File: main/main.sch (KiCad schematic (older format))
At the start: 0 parts

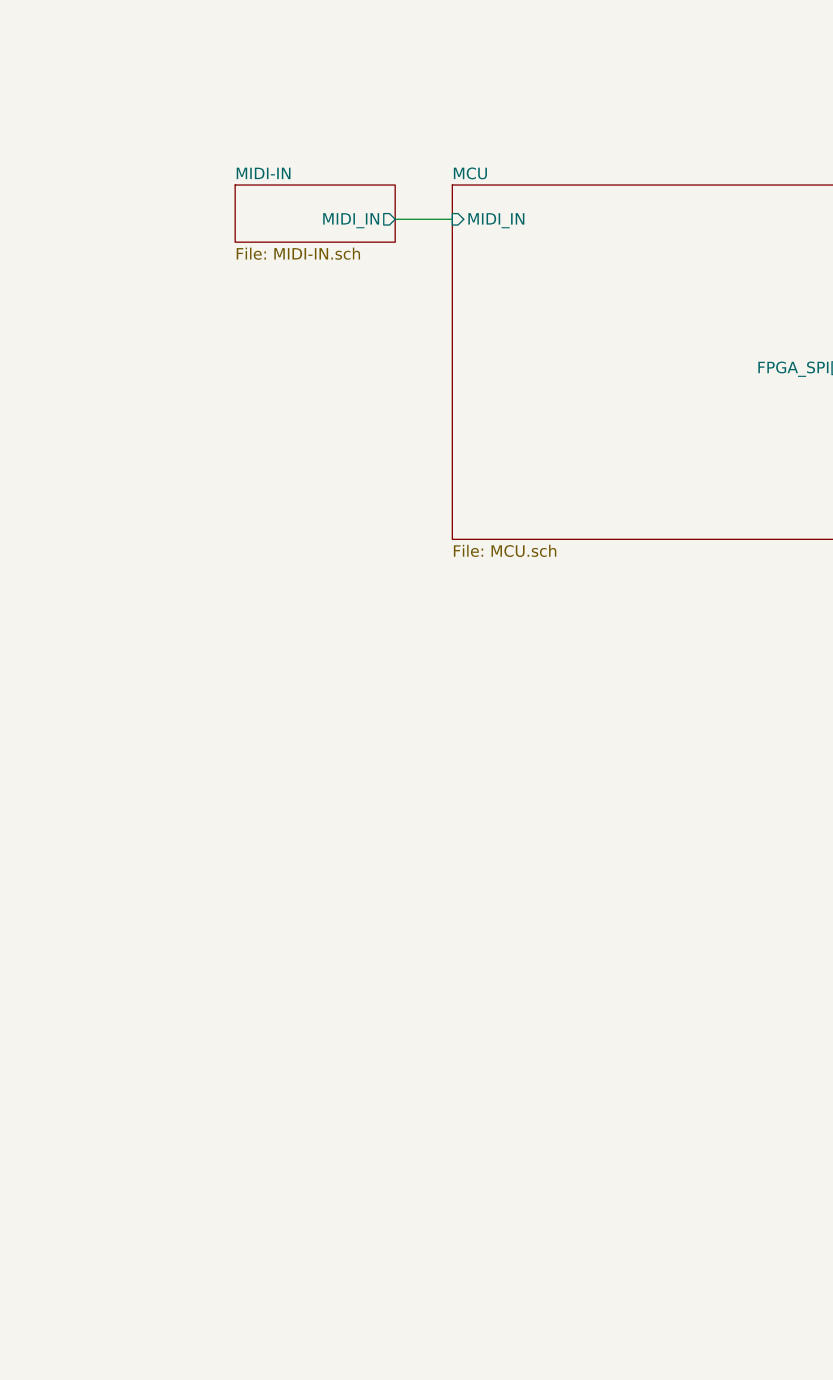
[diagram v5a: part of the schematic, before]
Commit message: Add the MCU we will be using, try setting up power connections
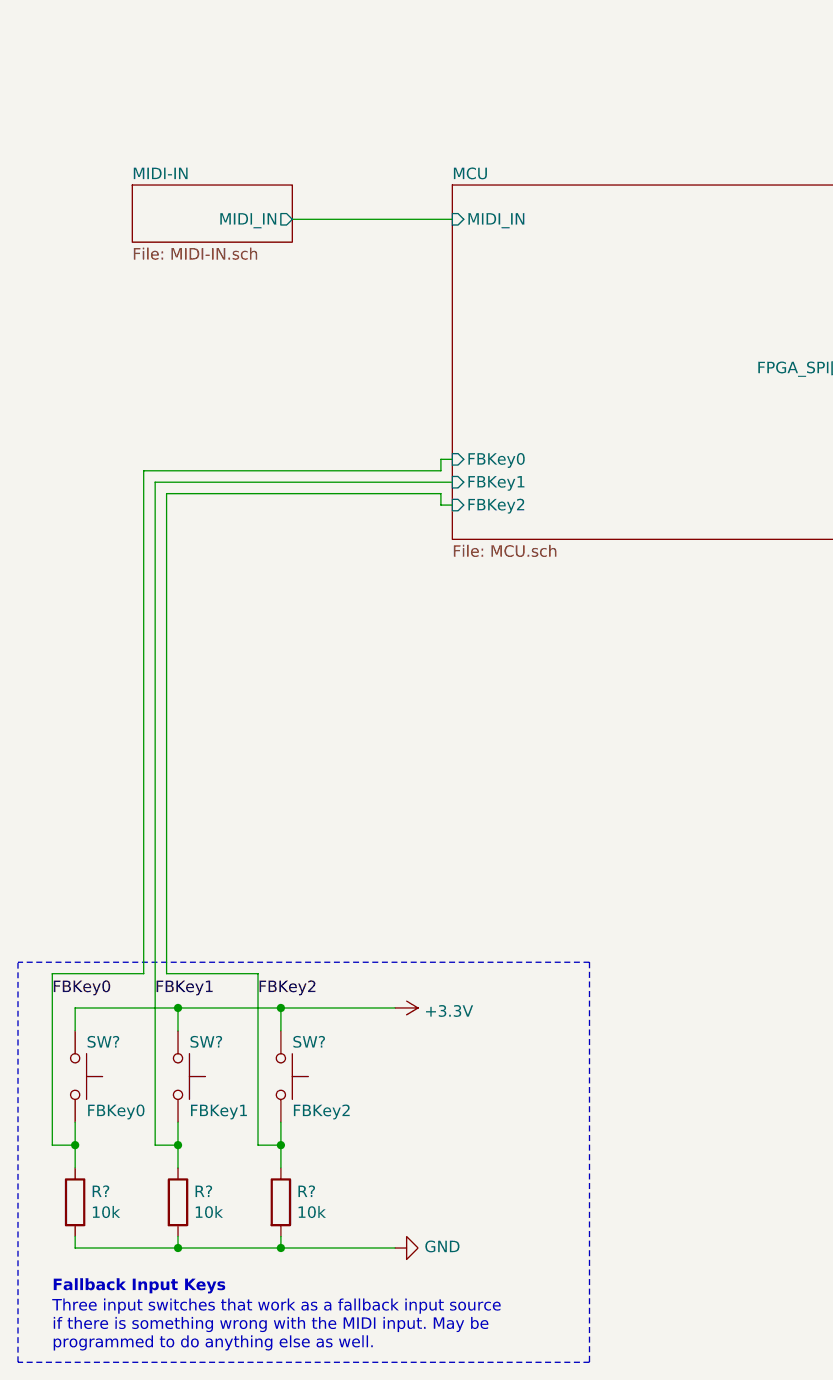
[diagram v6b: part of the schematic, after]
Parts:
- added R? (x3): 10k, symbol Device:R
- added SW?: FBKey0, symbol Switch:SW_Push
- added SW?: FBKey1, symbol Switch:SW_Push
- added SW?: FBKey2, symbol Switch:SW_Push
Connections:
- new net +3V3: SW?.1, SW?.1, SW?.1
- new net FBKey0: R?.1, SW?.2
- new net FBKey1: R?.1, SW?.2
- new net FBKey2: R?.1, SW?.2
- new net GND: R?.2, R?.2, R?.2
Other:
- note added: "Fallback Input Keys"
- note added: "Three input switches that work as a fallback input source\nif there is something wrong with the MIDI input. May be\nprogrammed to do anything else as well.\n"
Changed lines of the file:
@@
 $EndDescr
 $Sheet
-S 1500 2550 700  250
+S 1050 2550 700  250
 U 613F97F2
 F0 "MIDI-IN" 50
 F1 "MIDI-IN.sch" 50
-F2 "MIDI_IN" O R 2200 2700 50
+F2 "MIDI_IN" O R 1750 2700 50
 $EndSheet
 $Sheet
@@
 F2 "MIDI_IN" I L 2450 2700 50
 F3 "FPGA_SPI[0..3]" B R 4350 3350 50
-$EndSheet
-Wire Wire Line
-	2200 2700 2450 2700
+F4 "FBKey0" I L 2450 3750 50
+F5 "FBKey1" I L 2450 3850 50
+F6 "FBKey2" I L 2450 3950 50
+$EndSheet
+Wire Wire Line
+	1750 2700 2450 2700
 Wire Bus Line
 	4350 3350 5350 3350
@@
 F6 "DAC_MODE_LATCH" I L 8150 4850 50
 $EndSheet
+$Comp
+L Switch:SW_Push SW?
+U 1 1 6145369A
+P 800 6450
+F 0 "SW?" V 650 6500 50  0000 L CNN
+F 1 "FBKey0" V 950 6500 50  0000 L CNN
+F 2 "" H 800 6650 50  0001 C CNN
+F 3 "~" H 800 6650 50  0001 C CNN
+	1    800  6450
+	0    1    1    0
+$EndComp
+$Comp
+L Device:R R?
+U 1 1 61453C7F
+P 800 7000
+F 0 "R?" H 870 7046 50  0000 L CNN
+F 1 "10k" H 870 6955 50  0000 L CNN
+F 2 "" V 730 7000 50  0001 C CNN
+F 3 "~" H 800 7000 50  0001 C CNN
+	1    800  7000
+	1    0    0    -1
+$EndComp
+$Comp
+L Switch:SW_Push SW?
+U 1 1 6145516D
+P 1250 6450
+F 0 "SW?" V 1100 6500 50  0000 L CNN
+F 1 "FBKey1" V 1400 6500 50  0000 L CNN
+F 2 "" H 1250 6650 50  0001 C CNN
+F 3 "~" H 1250 6650 50  0001 C CNN
+	1    1250 6450
+	0    1    1    0
+$EndComp
+$Comp
+L Device:R R?
+U 1 1 61455173
+P 1250 7000
+F 0 "R?" H 1320 7046 50  0000 L CNN
+F 1 "10k" H 1320 6955 50  0000 L CNN
+F 2 "" V 1180 7000 50  0001 C CNN
+F 3 "~" H 1250 7000 50  0001 C CNN
+	1    1250 7000
+	1    0    0    -1
+$EndComp
+$Comp
+L Switch:SW_Push SW?
+U 1 1 61455E9E
+P 1700 6450
+F 0 "SW?" V 1550 6500 50  0000 L CNN
+F 1 "FBKey2" V 1850 6500 50  0000 L CNN
+F 2 "" H 1700 6650 50  0001 C CNN
+F 3 "~" H 1700 6650 50  0001 C CNN
+	1    1700 6450
+	0    1    1    0
+$EndComp
+$Comp
+L Device:R R?
+U 1 1 61455EA4
+P 1700 7000
+F 0 "R?" H 1770 7046 50  0000 L CNN
+F 1 "10k" H 1770 6955 50  0000 L CNN
+F 2 "" V 1630 7000 50  0001 C CNN
+F 3 "~" H 1700 7000 50  0001 C CNN
+	1    1700 7000
+	1    0    0    -1
+$EndComp
+Wire Wire Line
+	800  6250 800  6150
+Wire Wire Line
+	1250 6250 1250 6150
+Wire Wire Line
+	1700 6250 1700 6150
+Wire Wire Line
+	1700 6150 2200 6150
+$Comp
+L power:+3.3V #PWR?
+U 1 1 61456654
+P 2200 6150
+F 0 "#PWR?" H 2200 6000 50  0001 C CNN
+F 1 "+3.3V" V 2215 6278 50  0000 L CNN
+F 2 "" H 2200 6150 50  0001 C CNN
+F 3 "" H 2200 6150 50  0001 C CNN
+	1    2200 6150
+	0    1    1    0
+$EndComp
+$Comp
+L power:GND #PWR?
+U 1 1 61457106
+P 2200 7200
+F 0 "#PWR?" H 2200 6950 50  0001 C CNN
+F 1 "GND" V 2205 7072 50  0000 R CNN
+F 2 "" H 2200 7200 50  0001 C CNN
+F 3 "" H 2200 7200 50  0001 C CNN
+	1    2200 7200
+	0    -1   -1   0
+$EndComp
+Wire Wire Line
+	800  6850 800  6750
+Wire Wire Line
+	800  7200 800  7150
+Wire Wire Line
+	1250 7150 1250 7200
+Wire Wire Line
+	1700 7150 1700 7200
+Wire Wire Line
+	1700 7200 2200 7200
+Wire Wire Line
+	1250 6850 1250 6750
+Wire Wire Line
+	1700 6850 1700 6750
+Wire Wire Line
+	800  6750 700  6750
+Connection ~ 800  6750
+Wire Wire Line
+	800  6750 800  6650
+Wire Wire Line
+	1250 6750 1150 6750
+Connection ~ 1250 6750
+Wire Wire Line
+	1250 6750 1250 6650
+Wire Wire Line
+	1700 6750 1600 6750
+Connection ~ 1700 6750
+Wire Wire Line
+	1700 6750 1700 6650
+Text Label 700  6100 0    50   ~ 0
+FBKey0
+Text Label 1150 6100 0    50   ~ 0
+FBKey1
+Text Label 1600 6100 0    50   ~ 0
+FBKey2
+Wire Wire Line
+	800  7200 1250 7200
+Connection ~ 1700 7200
+Connection ~ 1250 7200
+Wire Wire Line
+	1250 7200 1700 7200
+Wire Wire Line
+	800  6150 1250 6150
+Connection ~ 1700 6150
+Connection ~ 1250 6150
+Wire Wire Line
+	1250 6150 1700 6150
+Text Notes 700  7400 0    50   ~ 10
+Fallback Input Keys
+Text Notes 700  7650 0    50   ~ 0
+Three input switches that work as a fallback input source\nif there is something wrong with the MIDI input. May be\nprogrammed to do anything else as well.\n
+Wire Notes Line
+	3050 5950 3050 7700
+Wire Notes Line
+	3050 7700 550  7700
+Wire Notes Line
+	550  7700 550  5950
+Wire Wire Line
+	700  6000 700  6750
+Wire Wire Line
+	1150 3850 2450 3850
+Wire Wire Line
+	1150 3850 1150 6750
+Wire Wire Line
+	1600 6000 1600 6750
+Wire Notes Line
+	3050 5950 550  5950
+Wire Wire Line
+	1100 3800 2400 3800
+Wire Wire Line
+	1200 3900 2400 3900
+Wire Wire Line
+	1100 6000 1100 3800
+Wire Wire Line
+	700  6000 1100 6000
+Wire Wire Line
+	1200 6000 1200 3900
+Wire Wire Line
+	1600 6000 1200 6000
+Wire Wire Line
+	2400 3900 2400 3950
+Wire Wire Line
+	2400 3950 2450 3950
+Wire Wire Line
+	2400 3800 2400 3750
+Wire Wire Line
+	2400 3750 2450 3750
 $EndSCHEMATC
